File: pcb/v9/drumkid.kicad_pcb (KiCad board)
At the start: 2 copper layers, 90 x 140 mm, 54 parts, among them J1 DIN-5_180degree, J2 DIN-5_180degree, J3 Conn_01x15, J4 Conn_01x15, J9 AudioJack3_Ground_Switch, SW1 SW_Push, SW2 SW_Push, SW3 SW_Push, SW4 SW_Push, SW5 SW_Push, SW6 SW_Push, SW7 SW_SPDT, SW8 SW_SPDT, U1 6N138

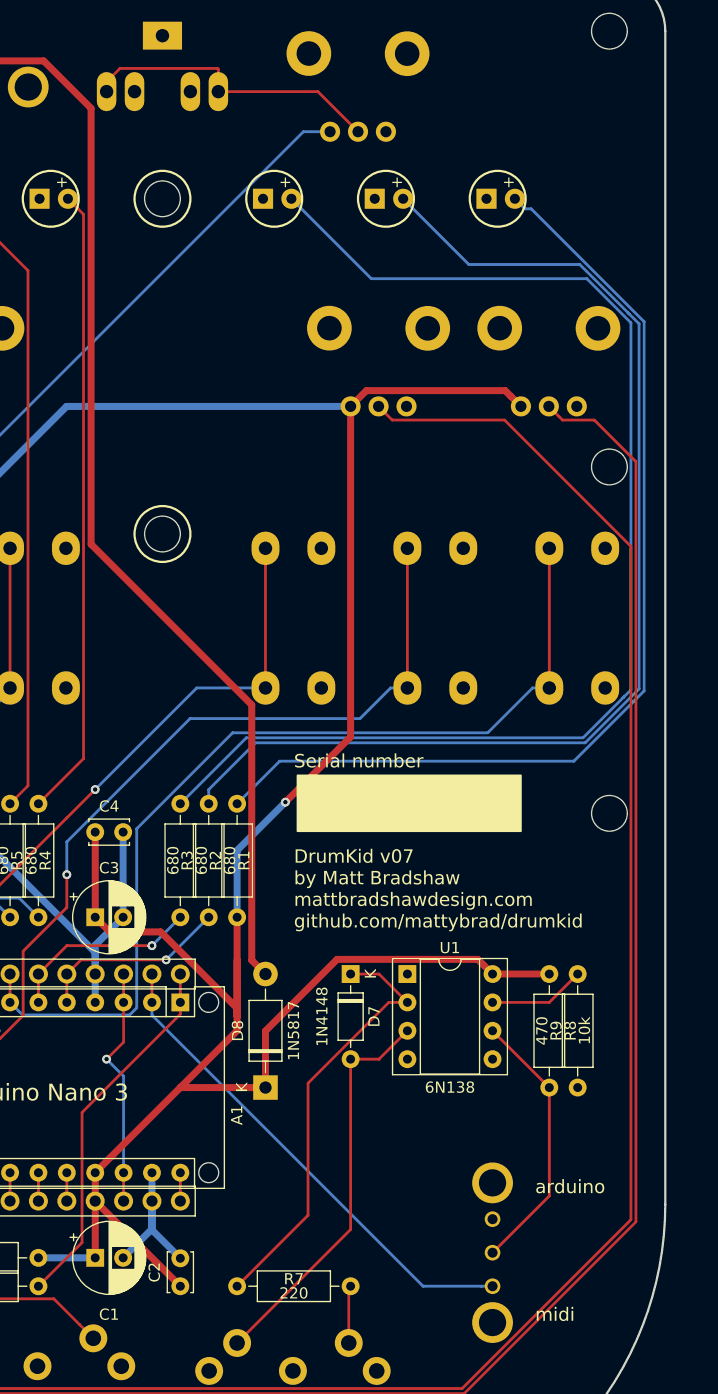
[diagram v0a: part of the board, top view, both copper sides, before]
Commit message: added v9, possible SMD version
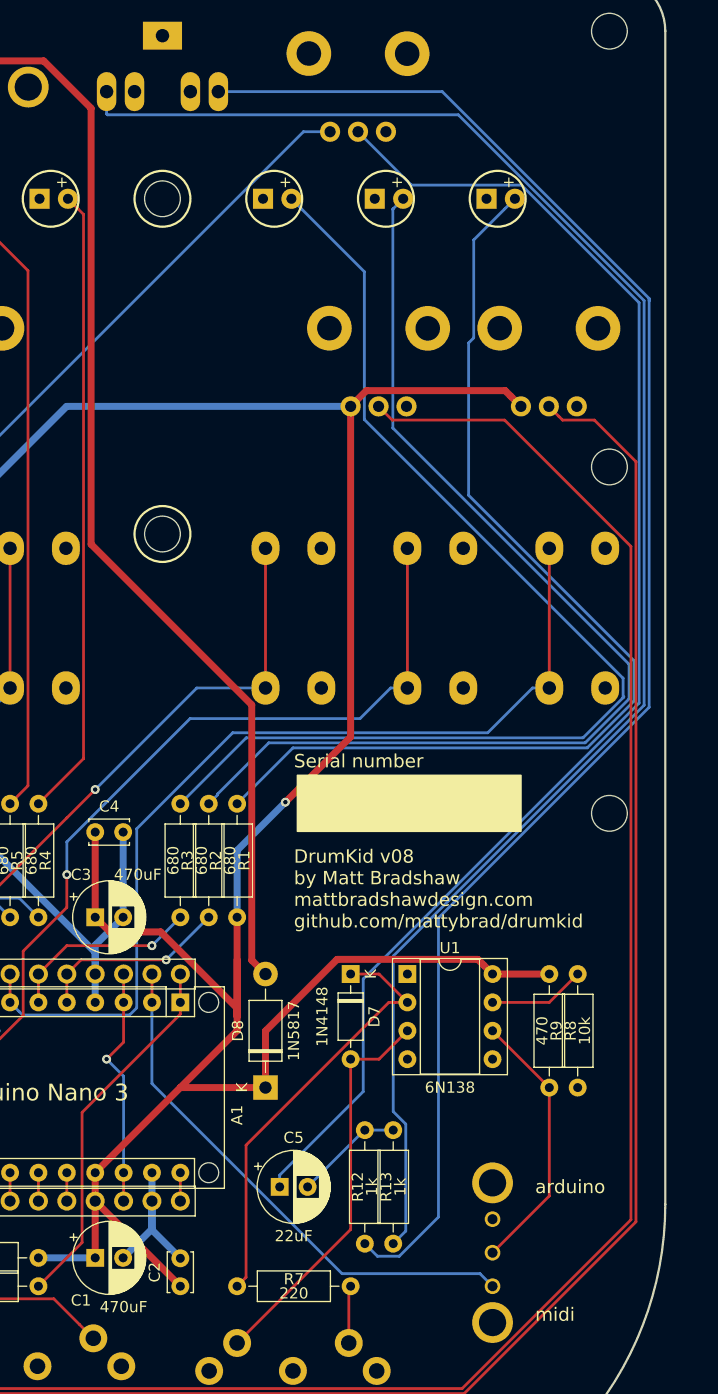
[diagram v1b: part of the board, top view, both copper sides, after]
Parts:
- added C5: 22uF, drumkidcustom:CP_Radial_D6.3mm_P2.50mm, F.Cu at (110.5, 138.4)
- added R12: 1k, drumkidcustom:R_Axial_DIN0207_L6.3mm_D2.5mm_P10.16mm_Horizontal, F.Cu at (118.1, 143.5)
- added R13: 1k, drumkidcustom:R_Axial_DIN0207_L6.3mm_D2.5mm_P10.16mm_Horizontal, F.Cu at (120.7, 143.5)
- C1, C3: value CP -> 470uF
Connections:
- J9 pad T: Net-(J9-PadR) -> Net-(J9-PadT)
- RV5 pad 2: Net-(J9-PadR) -> Net-(C5-Pad1)
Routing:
- net Net-(J9-PadT): track 0.00 -> 145.0 mm
- net Net-(J9-PadR): track 27.4 -> 152.5 mm
- net Net-(C5-Pad1): track 0.00 -> 123.9 mm
- net Net-(D3-Pad2): track 112.5 -> 100.6 mm
- net Net-(C5-Pad2): track 0.00 -> 9.76 mm
- net Net-(D2-Pad2): track 102.1 -> 95.4 mm
- net /DIGITAL_0: track 44.2 -> 47.8 mm
- net Net-(D1-Pad2): track 89.8 -> 92.1 mm
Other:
- board text added: "(change bank)"
- board text added: "(load)"
- board text added: "(save)"
- board text added: "DrumKid v08 by Matt Bradshaw mattbradshawdesign.com github.com/mattybrad/drumkid"
- board text removed: "DrumKid v07 by Matt Bradshaw mattbradshawdesign.com github.com/mattybrad/drumkid"
- board text removed: "change bank"
- board text removed: "load"
- board text removed: "save"

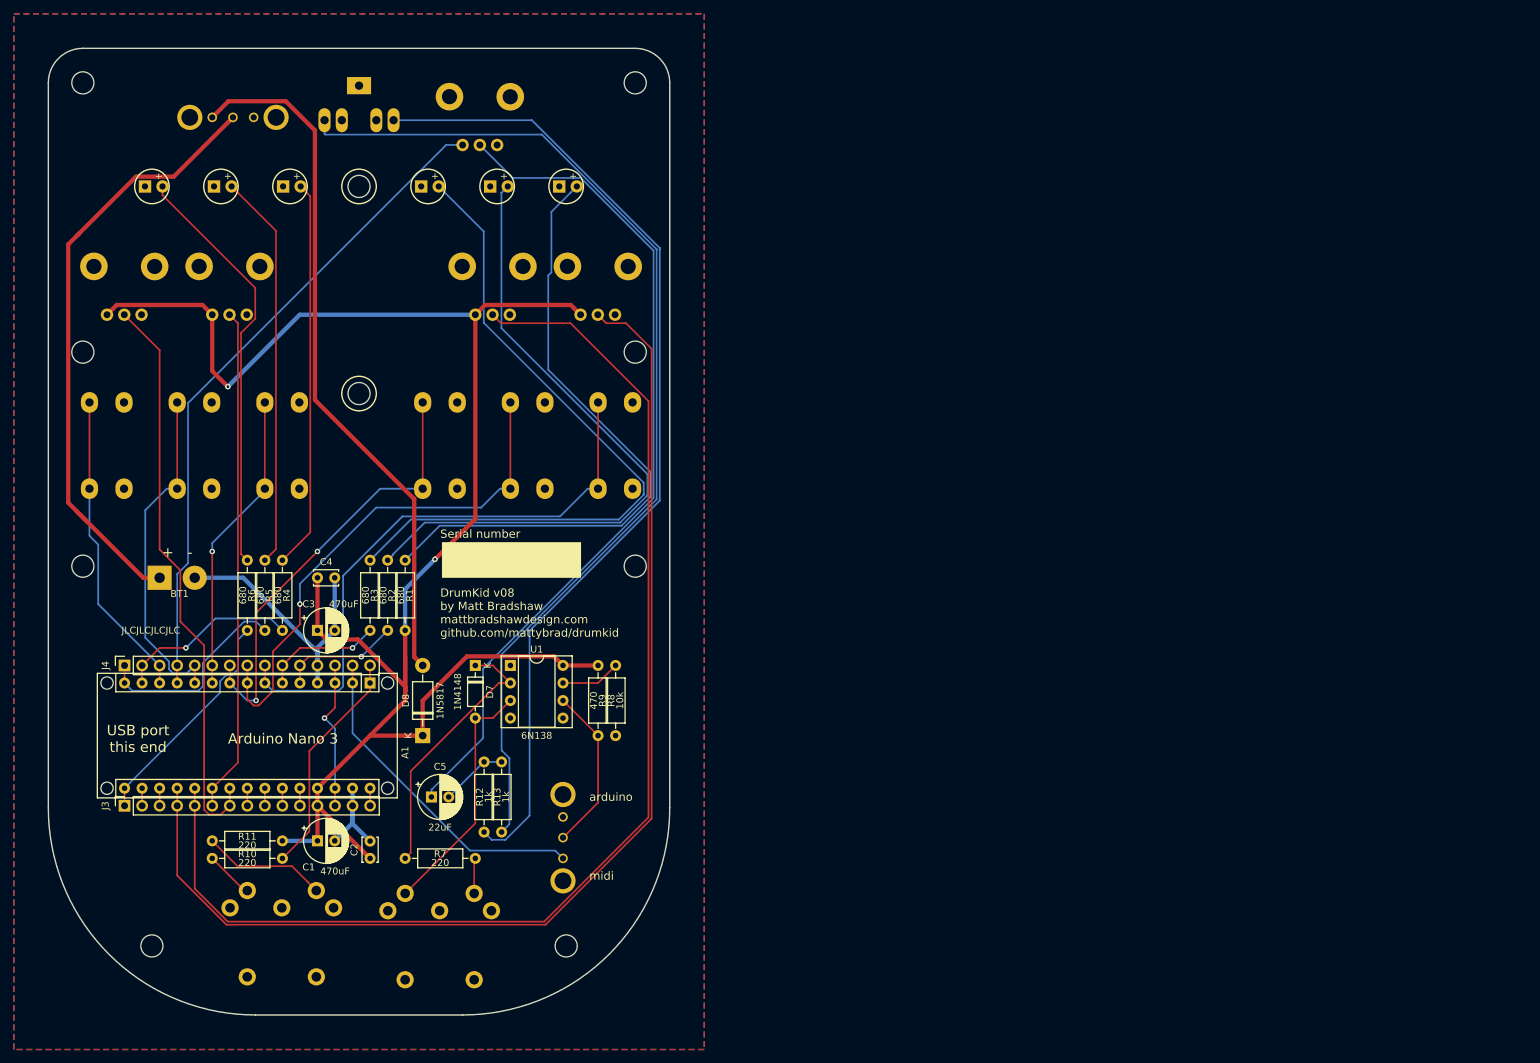
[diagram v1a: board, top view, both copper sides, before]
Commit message: added footprints for v9
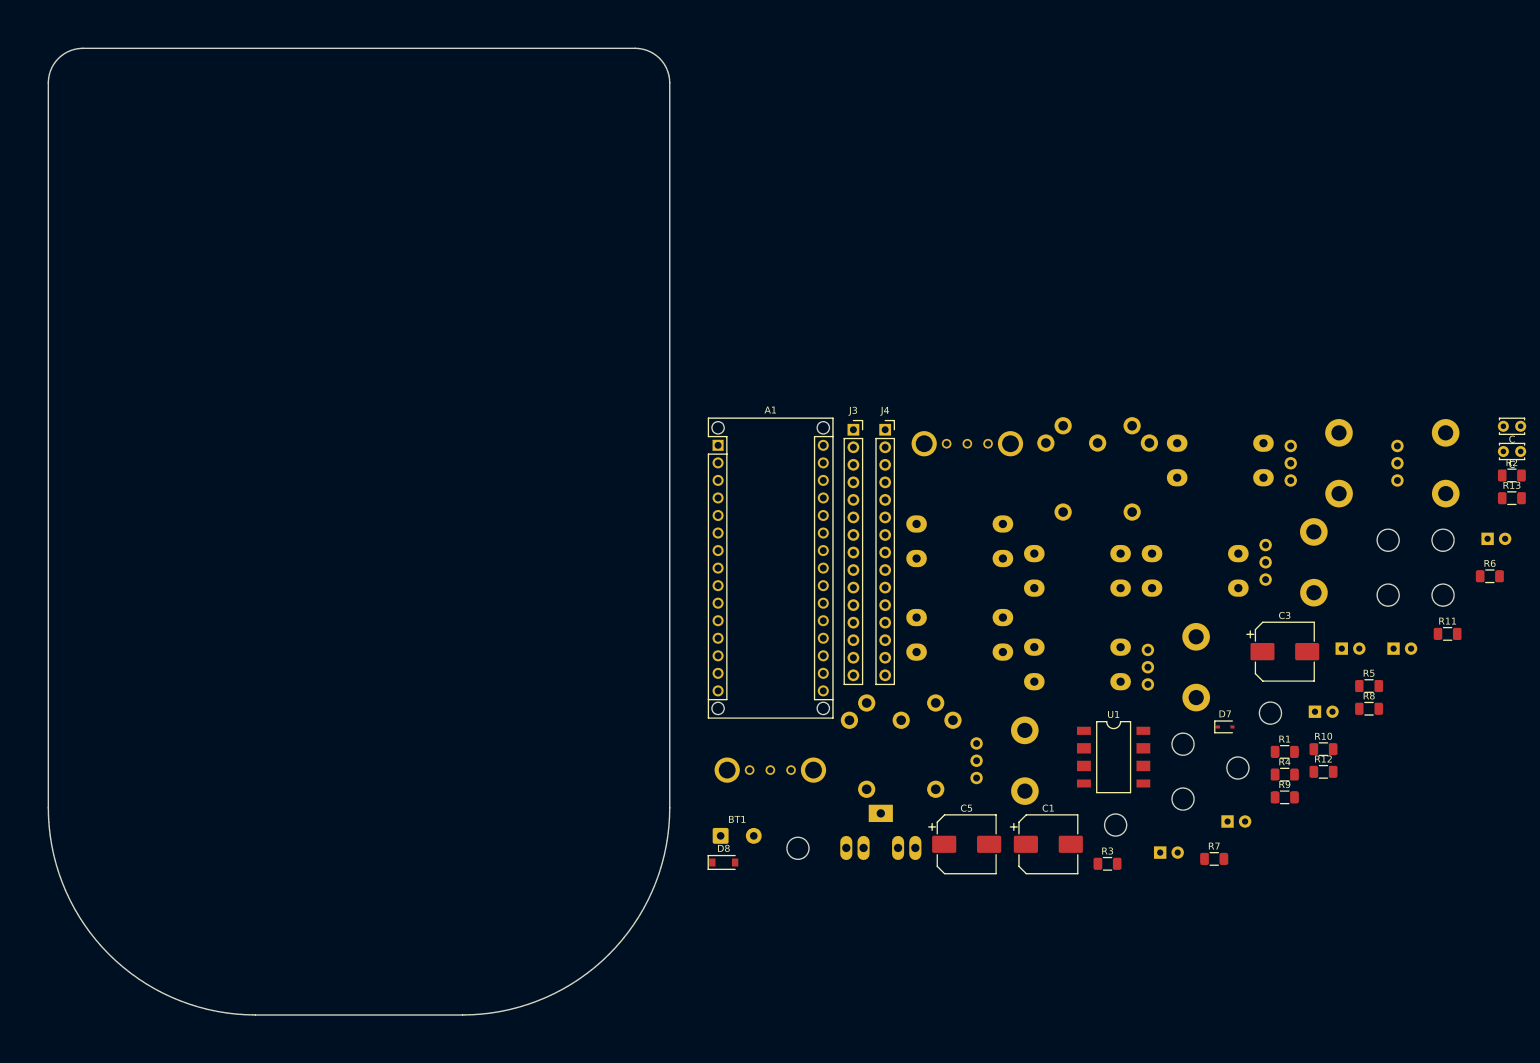
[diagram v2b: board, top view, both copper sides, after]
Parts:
- BT1: footprint Connector_Wire:SolderWirePad_1x02_P5.08mm_Drill1.5mm -> Connector_Wire:SolderWire-0.5sqmm_1x02_P4.8mm_D0.9mm_OD2.3mm
- C1, C3: footprint Capacitor_THT:CP_Radial_D6.3mm_P2.50mm -> Capacitor_SMD:CP_Elec_8x10
- C2, C4: footprint Capacitor_THT:C_Disc_D3.4mm_W2.1mm_P2.50mm -> drumkidcustom:C_Disc_D3.4mm_W2.1mm_P2.50mm
- C5: footprint drumkidcustom:CP_Radial_D6.3mm_P2.50mm -> Capacitor_SMD:CP_Elec_8x10
- D1, D2, D3, D4, D5, D6, H10, H9, J9, RV1, RV2, RV3, RV4, RV5, SW1, SW2, SW3, SW4, SW5, SW6, SW7: moved to F.Cu
- D7: footprint Diode_THT:D_DO-35_SOD27_P7.62mm_Horizontal -> Diode_SMD:D_SOD-323
- D8: value 1N5817 -> 1N4001; footprint Diode_THT:D_DO-41_SOD81_P10.16mm_Horizontal -> Diode_SMD:D_SOD-123
- R1, R10, R11, R12, R13, R2, R3, R4, R5, R6, R7, R8, R9: footprint drumkidcustom:R_Axial_DIN0207_L6.3mm_D2.5mm_P10.16mm_Horizontal -> Resistor_SMD:R_1206_3216Metric
- U1: footprint Package_DIP:DIP-8_W7.62mm_Socket -> Package_DIP:PowerIntegrations_SMD-8
- moved D6 201.0 mm to (263.4, 101.0)
- moved H9 200.1 mm to (257.0, 109.2)
- moved H2 189.1 mm to (249.1, 101.2)
- moved H1 185.9 mm to (219.3, 130.8)
- moved R11 181.4 mm to (257.7, 114.8)
- moved R6 180.0 mm to (263.8, 106.5), turned to 0 degrees
- moved C2 174.4 mm to (265.7, 88.4), turned to 0 degrees
- moved C4 173.2 mm to (265.7, 84.7)
- moved RV4 173.1 mm to (234.9, 92.6), turned to 0 degrees
- moved D4 167.7 mm to (238.4, 126.1)
- moved D5 167.6 mm to (216.0, 146.5)
- moved H7 165.2 mm to (257.0, 101.2)
- moved R2 163.3 mm to (267.0, 91.9), turned to 0 degrees
- moved R10 161.7 mm to (239.7, 131.5)
- moved R5 161.0 mm to (246.3, 122.4), turned to 0 degrees
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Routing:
- net VCC: track 256.7 -> 0.00 mm, vias 2 -> 0
- net /ANALOG_1: track 176.5 -> 0.00 mm
- net /ANALOG_0: track 168.5 -> 0.00 mm
- net Net-(J9-PadR): track 152.5 -> 0.00 mm
- net Net-(J9-PadT): track 145.0 -> 0.00 mm
- net Net-(C5-Pad1): track 123.9 -> 0.00 mm
- net Net-(D8-Pad2): track 101.5 -> 0.00 mm
- net Net-(D3-Pad2): track 100.6 -> 0.00 mm
- net /DIGITAL_9: track 96.4 -> 0.00 mm
- net Net-(D2-Pad2): track 95.4 -> 0.00 mm
- net Net-(D1-Pad2): track 92.1 -> 0.00 mm
- net Net-(BT1-Pad1): track 89.3 -> 0.00 mm
- net /DIGITAL_4: track 85.3 -> 0.00 mm
- net /ANALOG_3: track 83.5 -> 0.00 mm
- net /DIGITAL_5: track 75.7 -> 0.00 mm, vias 1 -> 0
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- removed copper zone on B.Cu, net GND
- removed copper zone on F.Cu, net GND
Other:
- board text removed: "(change bank)"
- board text removed: "(load)"
- board text removed: "(save)"
- board text removed: "+"
- board text removed: "+ -"
- board text removed: "0"
- board text removed: "1"
- board text removed: "1N4148"
- board text removed: "1N5817"
- board text removed: "6N138"
- board text removed: "Arduino Nano 3"
- board text removed: "DrumKid v08 by Matt Bradshaw mattbradshawdesign.com github.com/mattybrad/drumkid"
- board text removed: "JLCJLCJLCJLC"
- board text removed: "Serial number"
- board text removed: "USB port this end"
- board text removed: "a"
- board text removed: "a b c d"
- board text removed: "aleatoric drum machine"
- board text removed: "arduino"
- board text removed: "b"
- board text removed: "c"
- board text removed: "chance pitch drone beat"
- board text removed: "d"
- board text removed: "drumkid"
- board text removed: "midi"
- board text removed: "midi in"
- board text removed: "midi out"
- board text removed: "midpoint drop note tempo"
- board text removed: "range crop tuning swing"
- board text removed: "start/stop"
- board text removed: "tap tempo"
- board text removed: "zoom crush modulate beats/bar"

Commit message: v9 layout progress
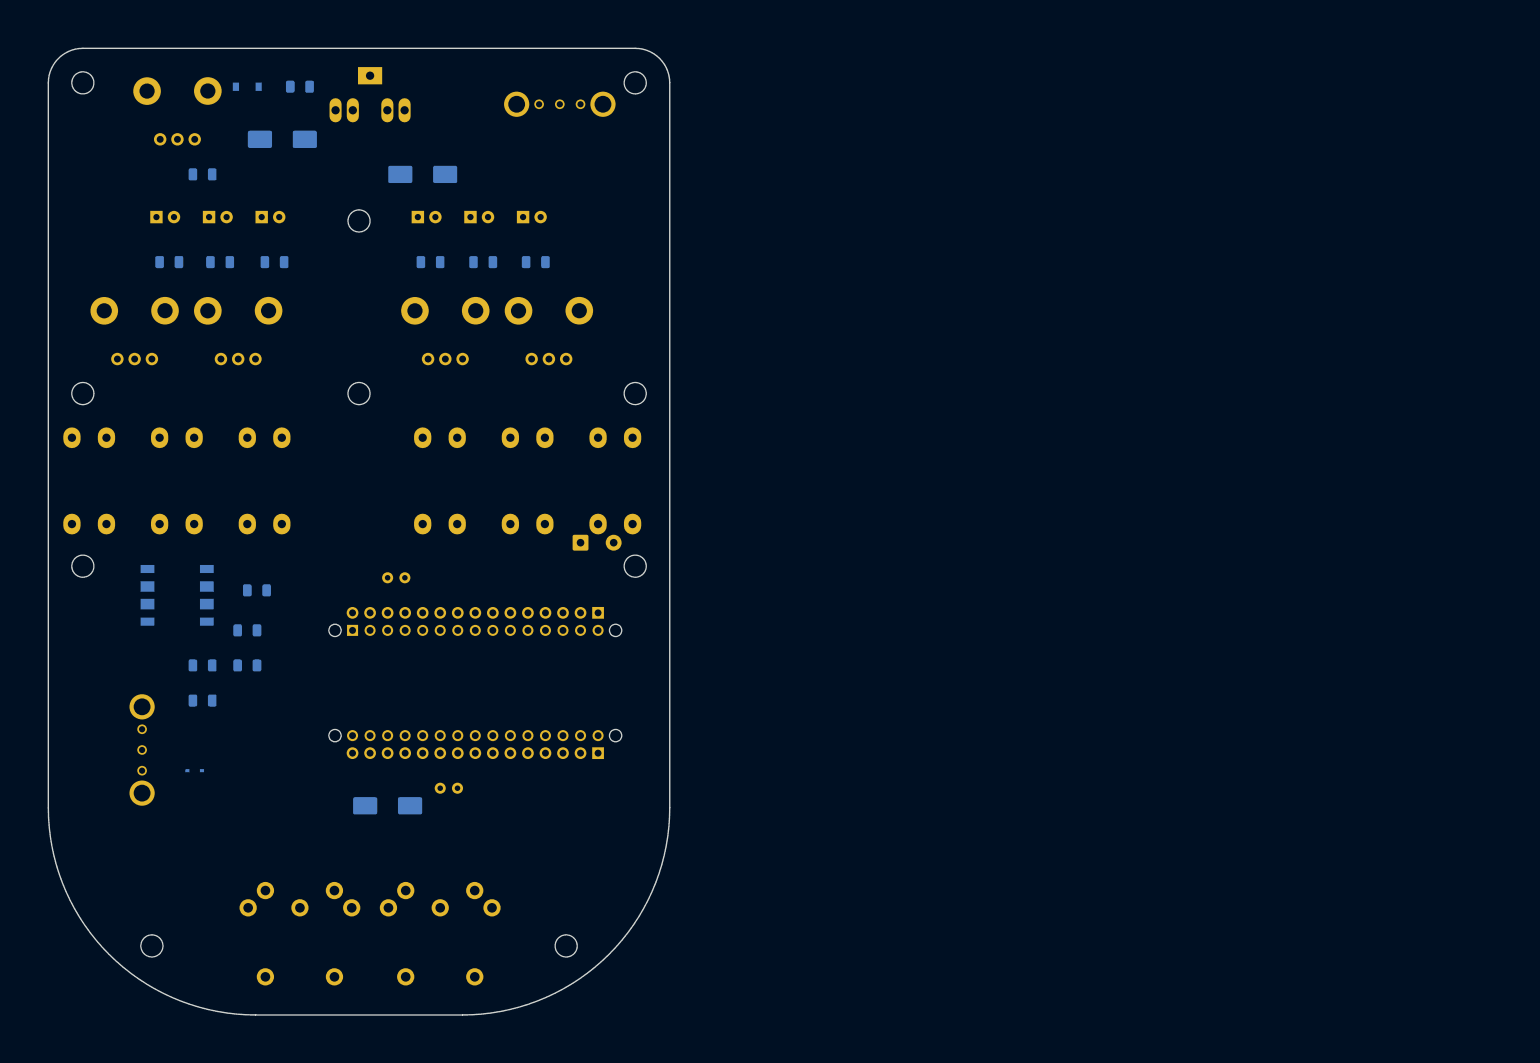
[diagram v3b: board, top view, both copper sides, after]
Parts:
- A1, BT1, C1, C2, C3, C4, C5, D7, D8, J1, J2, J3, J4, R1, R10, R11, R12, R13, R2, R3, R4, R5, R6, R7, R8, R9, SW8, U1: moved to B.Cu
- moved H7 196.0 mm to (70.0, 160.0)
- moved R13 195.3 mm to (77.3, 48.3)
- moved D1 189.8 mm to (70.7, 54.4)
- moved R2 189.6 mm to (79.9, 61.0)
- moved H1 185.9 mm to (60.0, 35.0)
- moved RV1 181.2 mm to (70.0, 75.0), turned to 90 degrees
- moved R11 180.6 mm to (77.3, 124.5)
- moved R12 178.4 mm to (91.4, 35.6)
- moved R1 176.4 mm to (72.5, 61.0)
- moved H5 173.3 mm to (60.0, 105.0)
- moved D2 171.5 mm to (78.3, 54.4)
- moved R8 169.1 mm to (77.3, 119.4)
- moved D3 168.5 mm to (85.9, 54.4)
- moved RV5 167.7 mm to (76.2, 43.2), turned to 90 degrees
- moved H9 166.1 mm to (100.0, 55.0)
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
